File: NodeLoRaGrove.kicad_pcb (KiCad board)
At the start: 2 copper layers, 40 x 50 mm, 44 parts, among them P1 PICKIT PROGRAMMER, P2 ICSP, P3 USB, P4 - Battery +, P5 A0, P6 D9, P7 I2C, P8 A2, SW1 RESET, U1 AP2112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

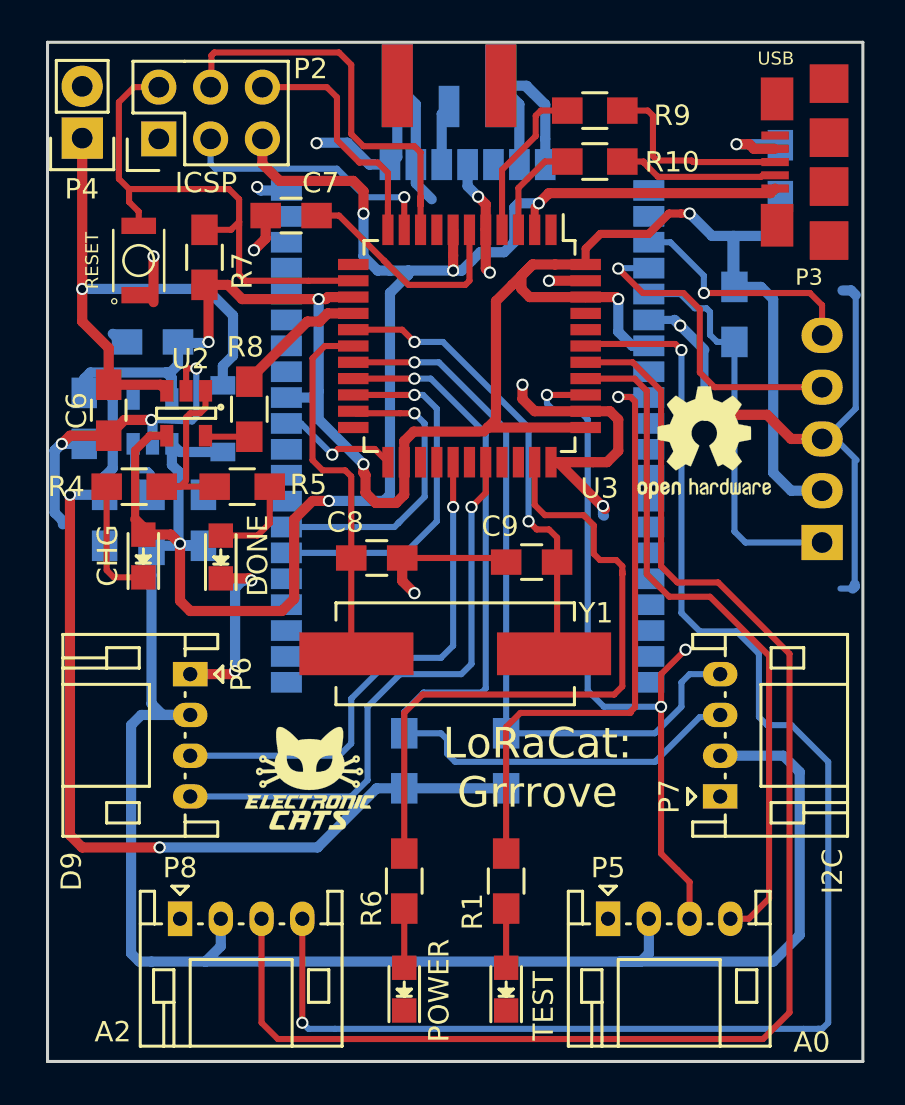
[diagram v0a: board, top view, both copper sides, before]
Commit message: Some vias and tracks fix
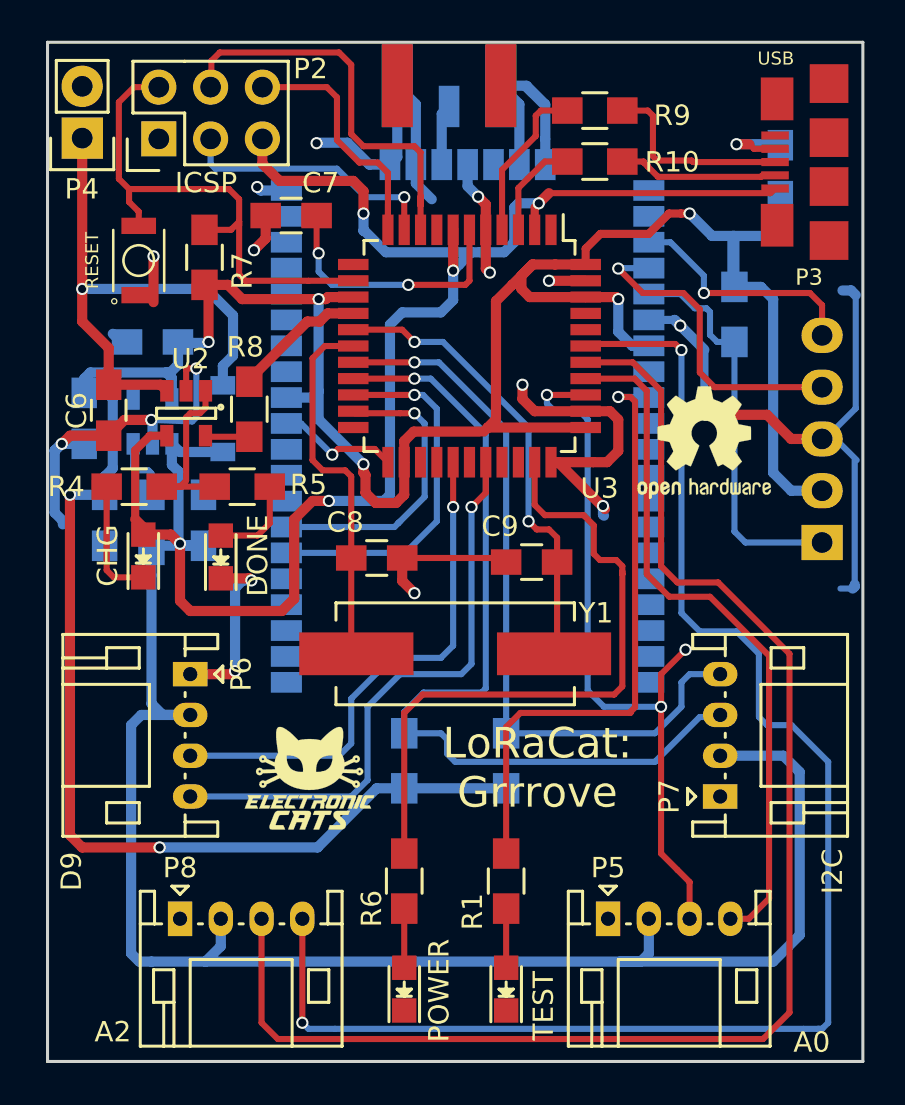
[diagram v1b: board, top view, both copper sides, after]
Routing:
- net VCC: track 162.0 -> 163.8 mm
- net Net-(C7-Pad1): track 11.8 -> 13.0 mm, vias 0 -> 2
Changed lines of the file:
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@@
     (links 120)
     (no_connects 0)
-    (area 124.724999 75.074999 164.875001 125.225001)
+    (area 123.825 65.740899 177.85 132.700001)
     (thickness 1.6)
     (drawings 11)
-    (tracks 618)
+    (tracks 622)
     (zones 0)
     (modules 44)
@@
   )
   (layers
-    (0 F.Cu signal hide)
-    (31 B.Cu signal hide)
+    (0 F.Cu signal)
+    (31 B.Cu signal)
     (32 B.Adhes user)
     (33 F.Adhes user)
@@
   (segment (start 144.5 78.298) (end 144.138262 78.659738) (width 0.5) (layer B.Cu) (net 1))
   (segment (start 144.138262 78.659738) (end 144.138262 81.15) (width 0.5) (layer B.Cu) (net 1))
-  (segment (start 160.492 80.376) (end 159.456998 80.376) (width 0.5) (layer F.Cu) (net 2))
+  (segment (start 160.492 80.376) (end 159.456998 80.376) (width 0.3) (layer F.Cu) (net 2))
   (segment (start 158.6 80.15) (end 159.230998 80.15) (width 0.5) (layer F.Cu) (net 2))
-  (segment (start 159.230998 80.15) (end 159.456998 80.376) (width 0.5) (layer F.Cu) (net 2))
+  (segment (start 159.230998 80.15) (end 159.456998 80.376) (width 0.3) (layer F.Cu) (net 2))
   (segment (start 134.8 101.55) (end 134.375736 101.55) (width 0.5) (layer B.Cu) (net 2))
   (segment (start 134.375736 101.55) (end 134 101.925736) (width 0.5) (layer B.Cu) (net 2))
@@
   (segment (start 142.2 100.45) (end 147.1 100.45) (width 0.3) (layer F.Cu) (net 2))
   (segment (start 147.1 100.45) (end 147.3 100.65) (width 0.3) (layer F.Cu) (net 2))
-  (segment (start 160.492 82.326) (end 160.26744 82.55056) (width 0.5) (layer F.Cu) (net 3))
-  (segment (start 160.26744 82.55056) (end 149.39944 82.55056) (width 0.5) (layer F.Cu) (net 3))
+  (segment (start 141.4 85.45) (end 145.6 85.45) (width 0.5) (layer B.Cu) (net 3))
+  (segment (start 145.6 85.45) (end 146.024264 85.45) (width 0.5) (layer B.Cu) (net 3))
+  (segment (start 144.7 86.35) (end 144.999999 86.050001) (width 0.5) (layer B.Cu) (net 3))
+  (segment (start 144.999999 86.050001) (end 145.6 85.45) (width 0.5) (layer B.Cu) (net 3))
+  (segment (start 142.2 88.4) (end 141.599999 89.000001) (width 0.5) (layer B.Cu) (net 3))
+  (segment (start 141.599999 89.000001) (end 141.599999 97.350001) (width 0.5) (layer B.Cu) (net 3))
+  (segment (start 144.1 88.4) (end 142.2 88.4) (width 0.5) (layer B.Cu) (net 3))
+  (segment (start 144.7 87.8) (end 144.1 88.4) (width 0.5) (layer B.Cu) (net 3))
+  (segment (start 144.7 86.35) (end 144.7 87.8) (width 0.5) (layer B.Cu) (net 3))
+  (segment (start 140.35 84.4) (end 141.4 85.45) (width 0.5) (layer B.Cu) (net 3))
+  (segment (start 140.3 83.55) (end 140.3 84.4) (width 0.5) (layer B.Cu) (net 3))
+  (segment (start 140.3 84.4) (end 140.35 84.4) (width 0.5) (layer B.Cu) (net 3))
+  (segment (start 160.492 82.326) (end 160.26744 82.55056) (width 0.3) (layer F.Cu) (net 3))
+  (segment (start 160.26744 82.55056) (end 149.39944 82.55056) (width 0.3) (layer F.Cu) (net 3))
   (segment (start 149.39944 82.55056) (end 148.9 83.05) (width 0.5) (layer F.Cu) (net 3))
   (segment (start 129.825 94.45) (end 130.65 94.45) (width 0.4) (layer F.Cu) (net 3))
@@
   (segment (start 147.7 84.95) (end 147.7 83.25) (width 0.5) (layer B.Cu) (net 3))
   (segment (start 147.2 85.45) (end 147.7 84.95) (width 0.5) (layer B.Cu) (net 3))
-  (segment (start 145.6 85.874264) (end 146.024264 85.45) (width 0.5) (layer B.Cu) (net 3))
   (segment (start 146.024264 85.45) (end 147.2 85.45) (width 0.5) (layer B.Cu) (net 3))
-  (segment (start 144.7 86.35) (end 145.124264 86.35) (width 0.5) (layer B.Cu) (net 3))
-  (segment (start 145.124264 86.35) (end 145.6 85.874264) (width 0.5) (layer B.Cu) (net 3))
   (segment (start 138.6 97.65) (end 137.8 97.65) (width 0.5) (layer F.Cu) (net 3))
   (segment (start 137.8 97.65) (end 136.9 98.55) (width 0.5) (layer F.Cu) (net 3))
@@
   (segment (start 129.9 107.6) (end 129.9 101.3) (width 0.5) (layer B.Cu) (net 3))
   (segment (start 129.9 101.3) (end 129.9 100.05) (width 0.5) (layer B.Cu) (net 3))
-  (segment (start 144.7 86.35) (end 142.5 86.35) (width 0.5) (layer B.Cu) (net 3))
-  (segment (start 142.5 86.35) (end 141.6 86.35) (width 0.5) (layer B.Cu) (net 3))
   (segment (start 141.3 97.65) (end 141.599999 97.350001) (width 0.5) (layer B.Cu) (net 3))
-  (segment (start 142.5 86.55) (end 142.5 86.35) (width 0.5) (layer B.Cu) (net 3))
-  (segment (start 141.599999 97.350001) (end 141.6 87.45) (width 0.5) (layer B.Cu) (net 3))
-  (segment (start 141.6 87.45) (end 142.5 86.55) (width 0.5) (layer B.Cu) (net 3))
-  (segment (start 140.3 85.65) (end 141 86.35) (width 0.5) (layer B.Cu) (net 3))
-  (segment (start 141 86.35) (end 141.6 86.35) (width 0.5) (layer B.Cu) (net 3))
-  (segment (start 140.3 83.55) (end 140.3 85.65) (width 0.5) (layer B.Cu) (net 3))
   (segment (start 140.3 82.45) (end 140.3 83.55) (width 0.5) (layer F.Cu) (net 3))
   (via (at 140.3 83.55) (size 0.6) (drill 0.4) (layers F.Cu B.Cu) (net 3))
@@
   (segment (start 127.8 91.95) (end 130.35 91.95) (width 0.5) (layer F.Cu) (net 5))
   (segment (start 130.35 91.95) (end 130.65 92.25) (width 0.5) (layer F.Cu) (net 5))
-  (segment (start 141.3 85.85) (end 139.1 83.65) (width 0.3) (layer F.Cu) (net 6))
-  (segment (start 139.1 83.65) (end 138 83.65) (width 0.3) (layer F.Cu) (net 6))
+  (segment (start 138.1 86.4) (end 138.75 87.05) (width 0.3) (layer B.Cu) (net 6))
+  (segment (start 138.75 87.05) (end 142.5 87.05) (width 0.3) (layer B.Cu) (net 6))
+  (segment (start 138.1 85.5) (end 138.1 86.4) (width 0.3) (layer B.Cu) (net 6))
+  (via (at 142.5 87.05) (size 0.6) (drill 0.4) (layers F.Cu B.Cu) (net 6))
+  (segment (start 138 83.65) (end 138 85.4) (width 0.3) (layer F.Cu) (net 6))
+  (segment (start 138 85.4) (end 138.1 85.5) (width 0.3) (layer F.Cu) (net 6))
+  (via (at 138.1 85.5) (size 0.6) (drill 0.4) (layers F.Cu B.Cu) (net 6))
   (segment (start 145.5 84.35) (end 145.5 86.85) (width 0.3) (layer F.Cu) (net 6))
   (segment (start 145.5 86.85) (end 145.3 87.05) (width 0.3) (layer F.Cu) (net 6))
   (segment (start 145.3 87.05) (end 142.5 87.05) (width 0.3) (layer F.Cu) (net 6))
-  (segment (start 142.5 87.05) (end 141.3 85.85) (width 0.3) (layer F.Cu) (net 6))
-  (segment (start 141.3 85.85) (end 141.5 86.05) (width 0.3) (layer F.Cu) (net 6))
   (segment (start 137.8 95.65) (end 137.8 90.65) (width 0.3) (layer F.Cu) (net 7))
   (segment (start 139.7 100.45) (end 139.7 96.45) (width 0.3) (layer F.Cu) (net 7))
@@
   (segment (start 142.3 84.35) (end 142.3 82.75) (width 0.3) (layer F.Cu) (net 17))
   (via (at 142.3 82.75) (size 0.6) (drill 0.4) (layers F.Cu B.Cu) (net 17))
-  (segment (start 143.1 84.35) (end 143.1 83.15) (width 0.3) (layer F.Cu) (net 18))
-  (segment (start 143.1 83.15) (end 143.1 82.7) (width 0.3) (layer F.Cu) (net 18))
-  (segment (start 143.1 80.55) (end 143.1 83.15) (width 0.3) (layer F.Cu) (net 18))
-  (segment (start 142.8 80.25) (end 143.1 80.55) (width 0.3) (layer F.Cu) (net 18))
-  (segment (start 140.3 80.25) (end 142.8 80.25) (width 0.3) (layer F.Cu) (net 18))
+  (segment (start 132.84 77.01) (end 132.84 76.06) (width 0.3) (layer F.Cu) (net 18))
+  (segment (start 139.1 75.65) (end 139.7 76.25) (width 0.3) (layer F.Cu) (net 18))
+  (segment (start 132.84 76.06) (end 133.25 75.65) (width 0.3) (layer F.Cu) (net 18))
   (segment (start 139.7 79.65) (end 140.3 80.25) (width 0.3) (layer F.Cu) (net 18))
+  (segment (start 142.8 80.25) (end 143.1 80.55) (width 0.3) (layer F.Cu) (net 18))
+  (segment (start 133.25 75.65) (end 139.1 75.65) (width 0.3) (layer F.Cu) (net 18))
   (segment (start 139.7 76.25) (end 139.7 79.65) (width 0.3) (layer F.Cu) (net 18))
-  (segment (start 139.1 75.65) (end 139.7 76.25) (width 0.3) (layer F.Cu) (net 18))
-  (segment (start 132.978686 75.65) (end 139.1 75.65) (width 0.3) (layer F.Cu) (net 18))
-  (segment (start 132.84 77.01) (end 132.84 75.788686) (width 0.3) (layer F.Cu) (net 18))
-  (segment (start 132.84 75.788686) (end 132.978686 75.65) (width 0.3) (layer F.Cu) (net 18))
+  (segment (start 140.3 80.25) (end 142.8 80.25) (width 0.3) (layer F.Cu) (net 18))
+  (segment (start 143.1 80.55) (end 143.1 83.15) (width 0.3) (layer F.Cu) (net 18))
+  (segment (start 143.1 84.35) (end 143.1 83.15) (width 0.3) (layer F.Cu) (net 18))
+  (segment (start 143.1 83.15) (end 143.1 82.7) (width 0.3) (layer F.Cu) (net 18))
   (segment (start 141 81.05) (end 141.5 81.55) (width 0.3) (layer F.Cu) (net 19))
   (segment (start 141.5 81.55) (end 141.5 84.35) (width 0.3) (layer F.Cu) (net 19))
